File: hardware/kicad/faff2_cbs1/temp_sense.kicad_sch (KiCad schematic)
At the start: 44 parts, among them J701 1752120, J702 1752120, U701 ADS1120

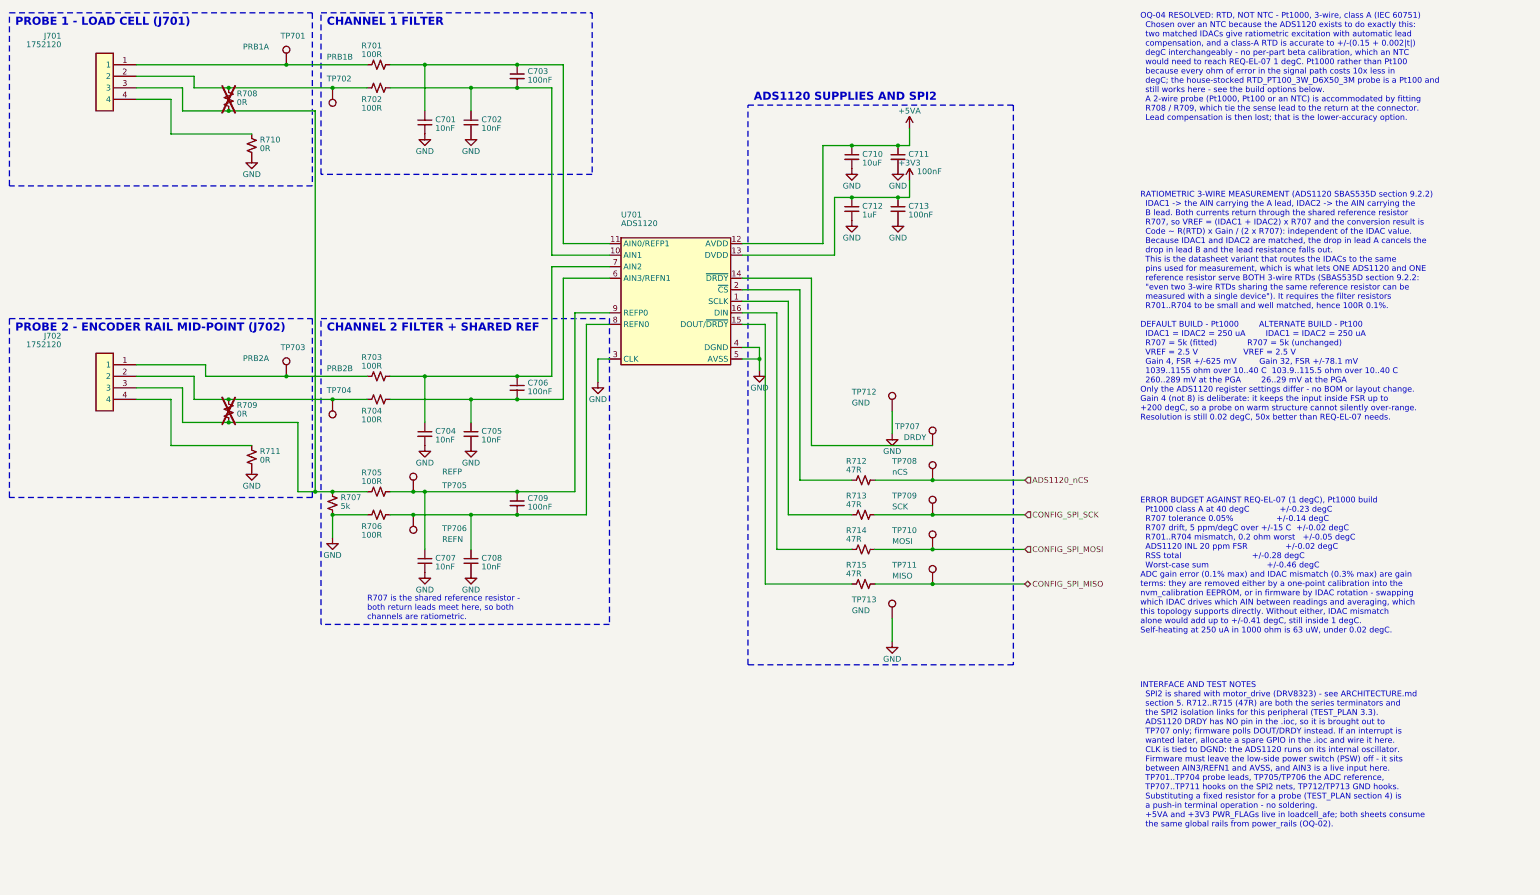
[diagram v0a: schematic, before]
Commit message: review r3 item 2: temp_sense SPI2 hooks become one keyed header, J703
Five hooks on the SPI2 nets meant five probe leads and five chances to slip a
clip off a 47R terminator. actuator-rev-afe.md section 7 had already recommended
this exact part for this exact sheet, so this applies a standing recommendation;
J502 and J603 are the two existing instances and the channel map copies J603 pin
for pin - CH0..CH4 on pins 1..5, CH5..CH7 no-connect, GND on 9 and 10. Tapped
MCU-side of R712..R715 so the bus stays visible with a link out. TP712/TP713
stay: they are the hooks the analyser's ground leads clip to.

It reaches its nets by local labels rather than wires - the five arrive at 7.62
pitch against 2.54 pins, so direct wiring is five doglegs. That is J502's idiom
and the netlist already shows it: loadcell_afe's SPI3 nets are /loadcell_afe/*
for the same reason. temp_sense's four bus nets move from /mcu/* to
/temp_sense/*: a rename with identical membership, and no board yet to disturb.

The block box grew from y=154.94 to 181.61 because a label must sit entirely
over its wire - 19 mm of run each side is 66 mm of cluster against a 58 mm box
whose left third carries U701's descending bundle. TP712's GND cluster went up
5.08 mm, which it needed regardless: its arrow tip sat exactly on the
ADS1120_nDRDY wire, no connection but it draws as one.

That defect exposed a fifth blind spot in the new checker, which had passed the
sheet clean: net labels and symbol bodies were only ever obstacles, never
subjects. Both are subjects now, with two exemptions - a body is excused from a
wire landing on its own pins (Sheet.pin_points, or all 283 power symbols
report), a label from the wire through its own anchor. And text and outlines get
different rules: text keeps 0.35 mm clearance, a body box is the bounding box of
a triangle so it counts only when penetrated, or when a wire runs inside it for
0.635 mm. That separates "wire through the arrow's tip" from "wire starts at the
arrow's empt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
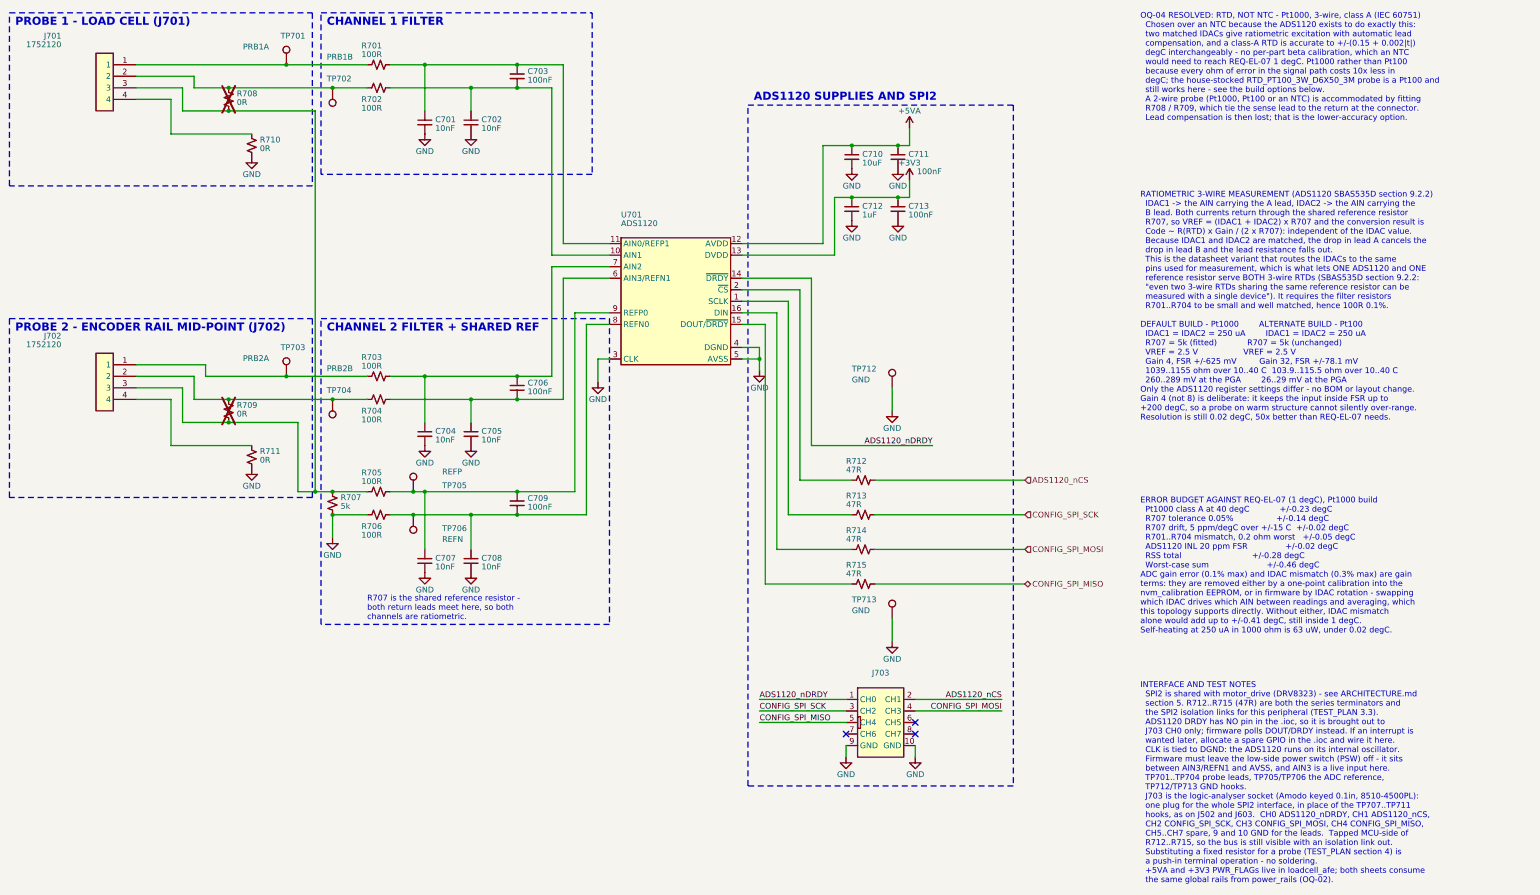
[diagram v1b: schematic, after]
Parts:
- removed TP707: DRDY, Amodo:KeystoneMiniatureTestLoop, symbol Amodo_Connectors:TestPointHook
- removed TP708: nCS, Amodo:KeystoneMiniatureTestLoop, symbol Amodo_Connectors:TestPointHook
- removed TP709: SCK, Amodo:KeystoneMiniatureTestLoop, symbol Amodo_Connectors:TestPointHook
- removed TP710: MOSI, Amodo:KeystoneMiniatureTestLoop, symbol Amodo_Connectors:TestPointHook
- removed TP711: MISO, Amodo:KeystoneMiniatureTestLoop, symbol Amodo_Connectors:TestPointHook
- added J703: 8510-4500PL, Amodo:8510-4500PL_LOGIC_TEST, symbol Amodo_Connectors:Header_Female_10-way_2-row_Straight_2.54mm_THT__KEYED_LOGIC_TE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
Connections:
- net ADS1120_nCS: now also J703.2 (CH1)
- net CONFIG_SPI_MISO: now also J703.5 (CH4)
- net CONFIG_SPI_MOSI: now also J703.4 (CH3)
- net CONFIG_SPI_SCK: now also J703.3 (CH2)
- net GND: now also J703.10 (GND), J703.9 (GND)
- net ADS1120_nDRDY: now reaches U701.14 (~{DRDY})
- net ADS1120_nDRDY: now also J703.1 (CH0)
- no-connect marks 0 -> 3
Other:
- note added: "INTERFACE AND TEST NOTES SPI2 is shared with motor_drive (DRV8323) - see ARCHITECTURE.md section 5. R712..R715 (47R) are both the series terminators and the SPI2 isolation links for this peripheral (TEST_PLAN 3.3). ADS1120 DRDY has NO pin in the .ioc, so it is brought out to J703 CH0 only; firmware polls DOUT/DRDY instead. If an interrupt is wanted later, allocate a spare GPIO in the .ioc and wir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"
- note removed: "INTERFACE AND TEST NOTES SPI2 is shared with motor_drive (DRV8323) - see ARCHITECTURE.md section 5. R712..R715 (47R) are both the series terminators and the SPI2 isolation links for this peripheral (TEST_PLAN 3.3). ADS1120 DRDY has NO pin in the .ioc, so it is brought out to TP707 only; firmware polls DOUT/DRDY instead. If an interrupt is wanted later, allocate a spare GPIO in the .ioc and wire i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"
- moved on the sheet: TP712

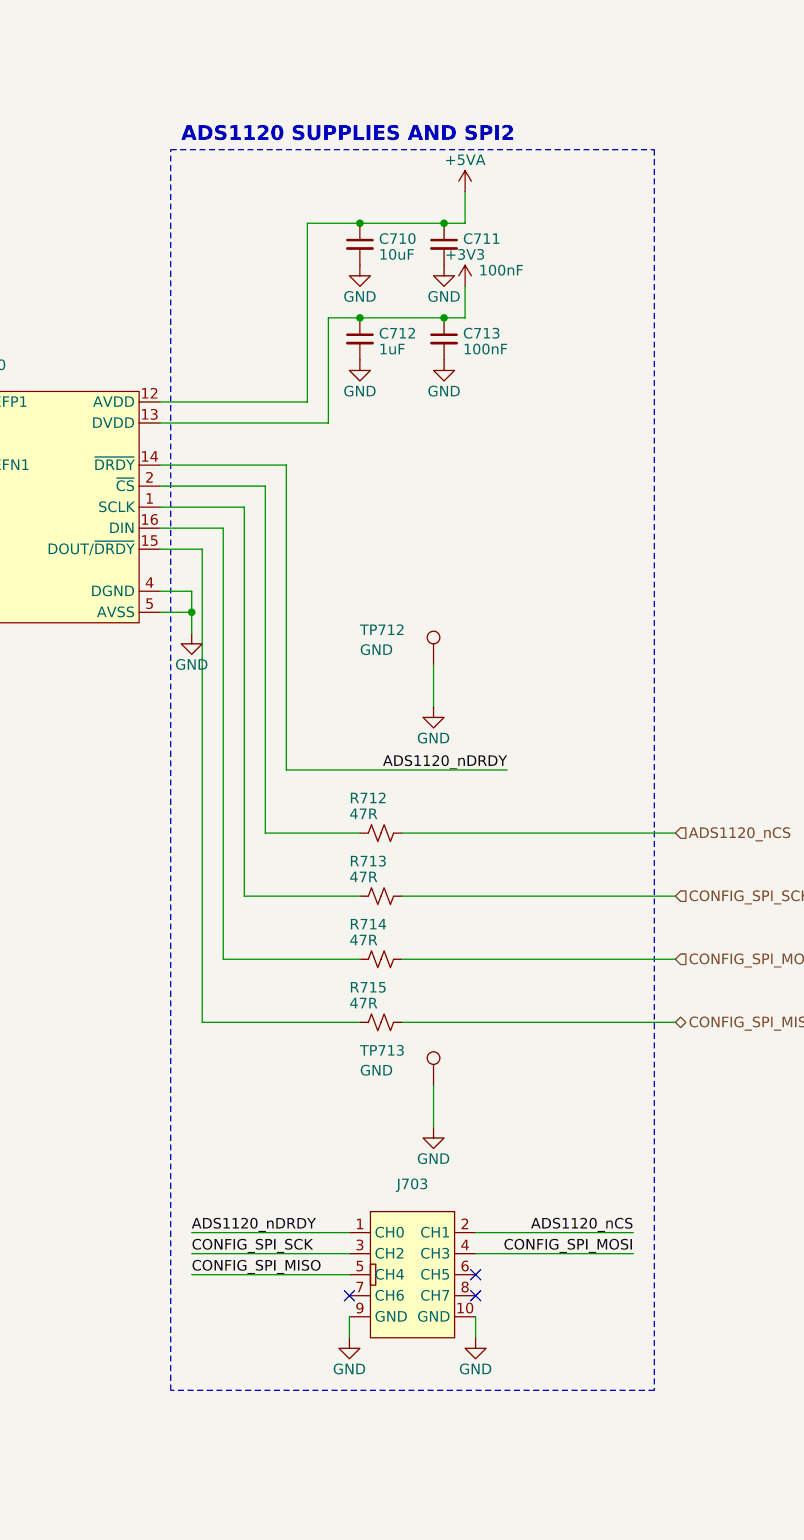
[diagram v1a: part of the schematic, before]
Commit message: review r3 item 4: respace every grazing placement, and rehome the TIM1 note
Round 2 left thirteen power-symbol names grazing something and pinned the
labels. Item 1's checker turned thirteen into sixty once labels and bodies
became subjects and the font model learned that block titles are bold 1.778 -
40% wider per character than the 1.27 it had assumed, which is how a 35 mm
title came back as 25. Fifty-seven are now clear. ERC 0/0 and node sets
identical: every change here is geometry.

The dominant defect, ten times over, is a power symbol's arrow with a vertex
exactly on a wire that runs past it and does not connect - the same thing the
captain screenshotted, nine more times. Each moves along its own stub: GND
arrows up, rail arrows down, because a rail arrow's name sits above it and
moving up only puts the text where the arrow was.

The rest: six bold titles wider than their block, eight notes and labels running
out through a border, twelve pinned names overlapped by a neighbour that moved
instead, and both 5 V PWR_FLAGs, which move onto the test-point stub below where
their 9.5 mm name has clear air.

Two checker corrections came out of doing the work. Fourteen findings were text
over its OWN conductor - a label on its wire with a branch of the same net
dropping through the text, which is what "the wire must extend under the entire
label" asks for; wire_nodes() groups segments into electrical nodes and excuses
the whole node. And field-against-field comparison had been lost in the
subject/obstacle rewrite - reference-against-value is the commonest defect there
is, and it went unnoticed until a render showed PWR_FLAG 0.86 mm inside a
neighbouring 100nF on a sheet the checker called clean.

The TIM1 note: round 2 recorded that nothing 47.6 x 8.7 fitted anywhere in
motor_drive block 4. With item 1's geometry that was wrong - 495 positions fit.
It now sits beside U1101's logic inputs, which is what it describes.

Three are left, both explained in the decisions file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
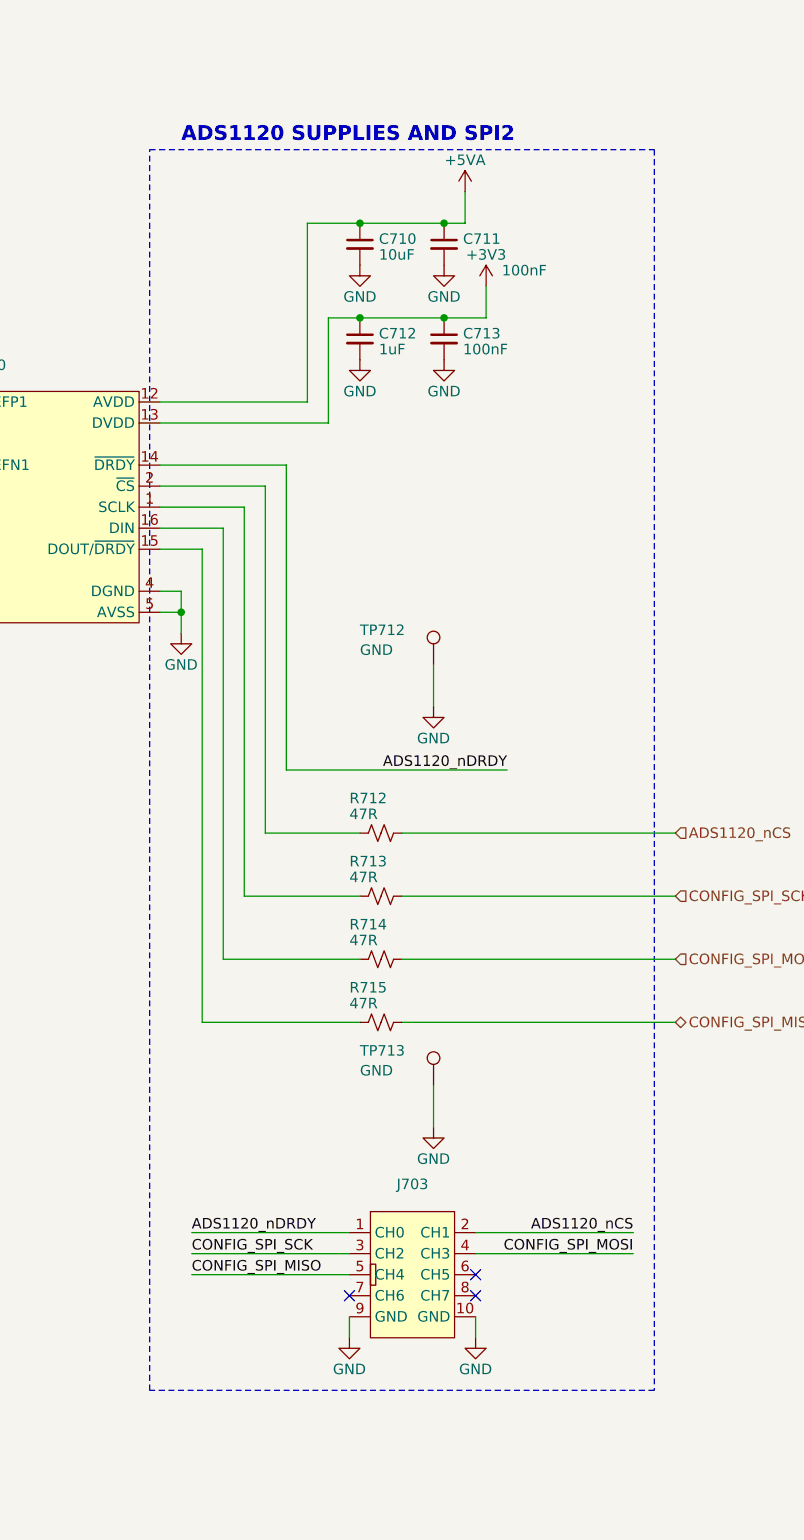
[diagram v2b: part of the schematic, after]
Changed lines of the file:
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@@
 		)
 		(property "Value" "100nF"
-			(at 217.555 46.355 0)
+			(at 220.34 46.35 0)
 			(do_not_autoplace yes)
 			(effects
@@
 	(symbol
 		(lib_id "Amodo_Symbols:+3V3")
-		(at 215.9 48.26 0)
+		(at 218.44 48.26 0)
 		(unit 1)
 		(exclude_from_sim no)
@@
 		(dnp no)
 		(property "Reference" "#PWR714"
-			(at 218.44 46.99 0)
+			(at 220.98 46.99 0)
 			(do_not_autoplace yes)
 			(effects
@@
 		)
 		(property "Value" "+3V3"
-			(at 215.9 44.45 0)
+			(at 218.44 44.45 0)
 			(do_not_autoplace yes)
 			(effects
@@
 		)
 		(property "Footprint" ""
-			(at 215.9 48.26 0)
+			(at 218.44 48.26 0)
 			(do_not_autoplace yes)
 			(effects
@@
 		)
 		(property "Datasheet" ""
-			(at 215.9 48.26 0)
+			(at 218.44 48.26 0)
 			(do_not_autoplace yes)
 			(effects
@@
 		)
 		(property "Description" ""
-			(at 215.9 48.26 0)
+			(at 218.44 48.26 0)
 			(do_not_autoplace yes)
 			(effects
@@
 		)
 		(property "SymLifecycle" "tested"
-			(at 215.9 48.26 0)
+			(at 218.44 48.26 0)
 			(do_not_autoplace yes)
 			(effects
@@
 	(symbol
 		(lib_id "Amodo_Symbols:GND")
-		(at 182.88 90.17 0)
+		(at 181.61 90.17 0)
 		(unit 1)
 		(exclude_from_sim no)
@@
 		(dnp no)
 		(property "Reference" "#PWR717"
-			(at 185.42 88.9 0)
+			(at 184.15 88.9 0)
 			(do_not_autoplace yes)
 			(effects
@@
 		)
 		(property "Value" "GND"
-			(at 182.88 93.98 0)
+			(at 181.61 93.98 0)
 			(do_not_autoplace yes)
 			(effects
@@
 		)
 		(property "Footprint" ""
-			(at 182.88 90.17 0)
+			(at 181.61 90.17 0)
 			(do_not_autoplace yes)
 			(effects
@@
 		)
 		(property "Datasheet" ""
-			(at 182.88 90.17 0)
+			(at 181.61 90.17 0)
 			(do_not_autoplace yes)
 			(effects
@@
 		)
 		(property "Description" "Power symbol creates a global label with name \"GND\" , ground"
-			(at 182.88 90.17 0)
+			(at 181.61 90.17 0)
 			(do_not_autoplace yes)
 			(effects
@@
 		)
 		(property "SymLifecycle" "tested"
-			(at 182.88 90.17 0)
+			(at 181.61 90.17 0)
 			(do_not_autoplace yes)
 			(effects
@@
 	)
 	(rectangle
-		(start 180.34 31.75)
+		(start 177.8 31.75)
 		(end 238.76 181.61)
 		(stroke
@@
 	(wire
 		(pts
-			(xy 215.9 48.26) (xy 215.9 52.07)
+			(xy 218.44 48.26) (xy 218.44 52.07)
 		)
 		(stroke
@@
 	(wire
 		(pts
-			(xy 215.9 52.07) (xy 213.36 52.07)
+			(xy 218.44 52.07) (xy 213.36 52.07)
 		)
 		(stroke
@@
 	(wire
 		(pts
-			(xy 179.07 85.09) (xy 182.88 85.09)
+			(xy 179.07 85.09) (xy 181.61 85.09)
 		)
 		(stroke
@@
 	(wire
 		(pts
-			(xy 182.88 85.09) (xy 182.88 87.63)
+			(xy 181.61 85.09) (xy 181.61 87.63)
 		)
 		(stroke
@@
 	(wire
 		(pts
-			(xy 182.88 87.63) (xy 182.88 90.17)
+			(xy 181.61 87.63) (xy 181.61 90.17)
 		)
 		(stroke
@@
 	(wire
 		(pts
-			(xy 179.07 87.63) (xy 182.88 87.63)
+			(xy 179.07 87.63) (xy 181.61 87.63)
 		)
 		(stroke
@@
 	)
 	(junction
-		(at 182.88 87.63)
+		(at 181.61 87.63)
 		(diameter 0)
 		(color 0 0 0 0)
